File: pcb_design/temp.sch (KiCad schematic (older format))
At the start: 3 parts

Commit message: Components placement, 3D models, updated some footprints to nominal IPC type
Signed-off-by: Marcos Chaparro <mchaparro@paltatech.com>
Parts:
- removed C41: 2.2u, CRF1:SMD-0603_c, symbol C-RESCUE-BLDC_4
- removed R1: NTC 10k, CRF1:SMD-0603_r, symbol R-RESCUE-BLDC_4
- removed R2: 10k, CRF1:SMD-0603_r, symbol R-RESCUE-BLDC_4
- added C41: 2.2u, IPC7351-Nominal:CAPC1608X55, symbol C-0603
- added R1: NTC 10k, IPC7351-Nominal:RESC1608X50, symbol R-0603
- added R2: 10k, IPC7351-Nominal:RESC1608X50, symbol R-0603
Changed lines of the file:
@@
 $Descr A4 11693 8268
 encoding utf-8
-Sheet 3 12
+Sheet 2 12
 Title "BLDC Driver 4.11"
 Date "21 aug 2015"
@@
 $EndDescr
 $Comp
-L R-RESCUE-BLDC_4 R1
-U 1 1 5426DA2F
-P 4400 3400
-F 0 "R1" V 4480 3400 40  0000 C CNN
-F 1 "NTC 10k" V 4407 3401 40  0000 C CNN
-F 2 "CRF1:SMD-0603_r" V 4330 3400 30  0001 C CNN
-F 3 "" H 4400 3400 30  0000 C CNN
-	1    4400 3400
+L VCC #PWR16
+U 1 1 5426DB11
+P 4400 3350
+F 0 "#PWR16" H 4400 3450 30  0001 C CNN
+F 1 "VCC" H 4400 3450 30  0000 C CNN
+F 2 "" H 4400 3350 60  0000 C CNN
+F 3 "" H 4400 3350 60  0000 C CNN
+	1    4400 3350
 	1    0    0    -1
 $EndComp
 $Comp
-L R-RESCUE-BLDC_4 R2
-U 1 1 5426DAA6
-P 4400 4100
-F 0 "R2" V 4480 4100 40  0000 C CNN
-F 1 "10k" V 4407 4101 40  0000 C CNN
-F 2 "CRF1:SMD-0603_r" V 4330 4100 30  0001 C CNN
-F 3 "" H 4400 4100 30  0000 C CNN
-	1    4400 4100
-	1    0    0    -1
-$EndComp
-$Comp
-L C-RESCUE-BLDC_4 C41
-U 1 1 5426DADD
-P 4150 4100
-F 0 "C41" H 4150 4200 40  0000 L CNN
-F 1 "2.2u" H 4156 4015 40  0000 L CNN
-F 2 "CRF1:SMD-0603_c" H 4188 3950 30  0001 C CNN
-F 3 "" H 4150 4100 60  0000 C CNN
-	1    4150 4100
-	1    0    0    -1
-$EndComp
-$Comp
-L VCC #PWR019
-U 1 1 5426DB11
-P 4400 3050
-F 0 "#PWR019" H 4400 3150 30  0001 C CNN
-F 1 "VCC" H 4400 3150 30  0000 C CNN
-F 2 "" H 4400 3050 60  0000 C CNN
-F 3 "" H 4400 3050 60  0000 C CNN
-	1    4400 3050
-	1    0    0    -1
-$EndComp
-$Comp
-L GND-RESCUE-BLDC_4 #PWR020
+L GND-RESCUE-BLDC_4 #PWR17
 U 1 1 5426DB25
-P 4400 4600
-F 0 "#PWR020" H 4400 4600 30  0001 C CNN
-F 1 "GND" H 4400 4530 30  0001 C CNN
-F 2 "" H 4400 4600 60  0000 C CNN
-F 3 "" H 4400 4600 60  0000 C CNN
-	1    4400 4600
+P 4400 4200
+F 0 "#PWR17" H 4400 4200 30  0001 C CNN
+F 1 "GND" H 4400 4130 30  0001 C CNN
+F 2 "" H 4400 4200 60  0000 C CNN
+F 3 "" H 4400 4200 60  0000 C CNN
+	1    4400 4200
 	1    0    0    -1
 $EndComp
 Wire Wire Line
-	4400 4350 4400 4600
+	4400 4050 4400 4200
 Wire Wire Line
-	4150 4300 4150 4450
-Wire Wire Line
-	4150 4450 4400 4450
-Connection ~ 4400 4450
+	4150 4150 4400 4150
+Connection ~ 4400 4150
 Wire Wire Line
 	4400 3650 4400 3850
 Wire Wire Line
 	4150 3750 4550 3750
-Wire Wire Line
-	4150 3750 4150 3900
 Connection ~ 4400 3750
 Wire Wire Line
-	4400 3050 4400 3150
+	4400 3350 4400 3450
 Text HLabel 4550 3750 2    60   Input ~ 0
 Temp
+$Comp
+L R-0603 R2
+U 1 1 588BA5AA
+P 4400 3950
+F 0 "R2" H 4463 3996 50  0000 L CNN
+F 1 "10k" H 4463 3905 50  0000 L CNN
+F 2 "IPC7351-Nominal:RESC1608X50" H 4400 3950 50  0001 C CNN
+F 3 "" H 4400 4000 60  0000 C CNN
+F 4 "RES SMD 1k 5% [0603]" H 5150 4500 60  0001 C CNN "BOM"
+	1    4400 3950
+	1    0    0    -1
+$EndComp
+$Comp
+L R-0603 R1
+U 1 1 588BA6A5
+P 4400 3550
+F 0 "R1" H 4463 3596 50  0000 L CNN
+F 1 "NTC 10k" H 4463 3505 50  0000 L CNN
+F 2 "IPC7351-Nominal:RESC1608X50" H 4400 3550 50  0001 C CNN
+F 3 "" H 4400 3600 60  0000 C CNN
+F 4 "RES SMD 1k 5% [0603]" H 5150 4100 60  0001 C CNN "BOM"
+	1    4400 3550
+	1    0    0    -1
+$EndComp
+$Comp
+L C-0603 C41
+U 1 1 588BA7A2
+P 4150 3950
+F 0 "C41" H 4263 3996 50  0000 L CNN
+F 1 "2.2u" H 4263 3905 50  0000 L CNN
+F 2 "IPC7351-Nominal:CAPC1608X55" H 4150 3950 50  0001 C CNN
+F 3 "" H 4140 3925 60  0000 C CNN
+F 4 "CAP MLCC 100pF C0G 50V 5% [0603]" H 4950 4500 60  0001 C CNN "BOM"
+	1    4150 3950
+	-1   0    0    -1
+$EndComp
+Wire Wire Line
+	4150 3850 4150 3750
+Wire Wire Line
+	4150 4050 4150 4150
 $EndSCHEMATC

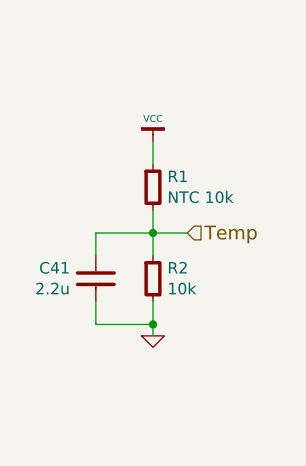
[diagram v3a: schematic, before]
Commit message: Added lp filters, fuses, tvs and power symbols
Signed-off-by: Marcos Chaparro <mchaparro@paltatech.com>
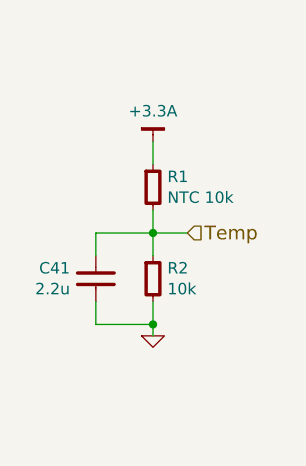
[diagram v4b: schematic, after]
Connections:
- net VCC renamed +3.3A
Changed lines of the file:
@@
 $EndDescr
-$Comp
-L VCC #PWR19
-U 1 1 5426DB11
-P 4400 3350
-F 0 "#PWR19" H 4400 3450 30  0001 C CNN
-F 1 "VCC" H 4400 3450 30  0000 C CNN
-F 2 "" H 4400 3350 60  0000 C CNN
-F 3 "" H 4400 3350 60  0000 C CNN
-	1    4400 3350
-	1    0    0    -1
-$EndComp
 $Comp
 L GND-RESCUE-BLDC_4 #PWR20
@@
 Wire Wire Line
 	4150 4050 4150 4150
+$Comp
+L +3.3A #PWR?
+U 1 1 588BA405
+P 4400 3350
+F 0 "#PWR?" H 0   100 30  0001 C CNN
+F 1 "+3.3A" H 4400 3483 50  0000 C CNN
+F 2 "" H 0   50  60  0000 C CNN
+F 3 "" H 0   50  60  0000 C CNN
+	1    4400 3350
+	1    0    0    -1
+$EndComp
 $EndSCHEMATC
